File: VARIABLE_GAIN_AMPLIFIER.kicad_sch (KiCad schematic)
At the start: 33 parts, among them IC35 ${DEVICE}

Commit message: Rerouted PCB Logic part
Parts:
- renumbered C94 to C601, C95 to C602, C96 to C603, C97 to C604, C98 to C605, C99 to C606, C100 to C607, C101 to C608, C102 to C609, C103 to C610, C104 to C611, C105 to C612, C106 to C613, C107 to C614, C108 to C615, C109 to C616, C110 to C617, C621 to C619, C619 to C620, C620 to C621, FL3 to FL601, FL4 to FL602, IC35 to IC601, R73 to R601, R74 to R602, R75 to R603, R76 to R604, R77 to R605, R78 to R606, TR5 to TR601, TR6 to TR602

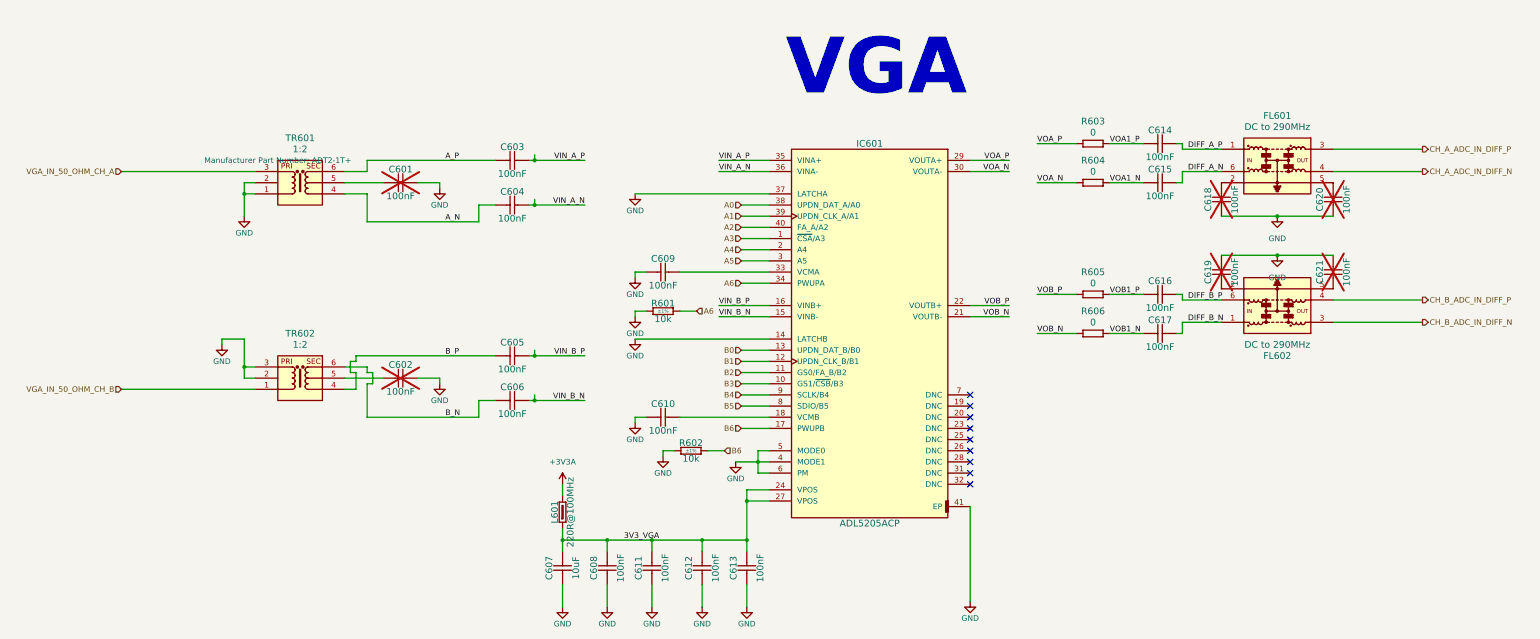
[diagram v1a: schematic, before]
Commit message: Inverted the VGA output
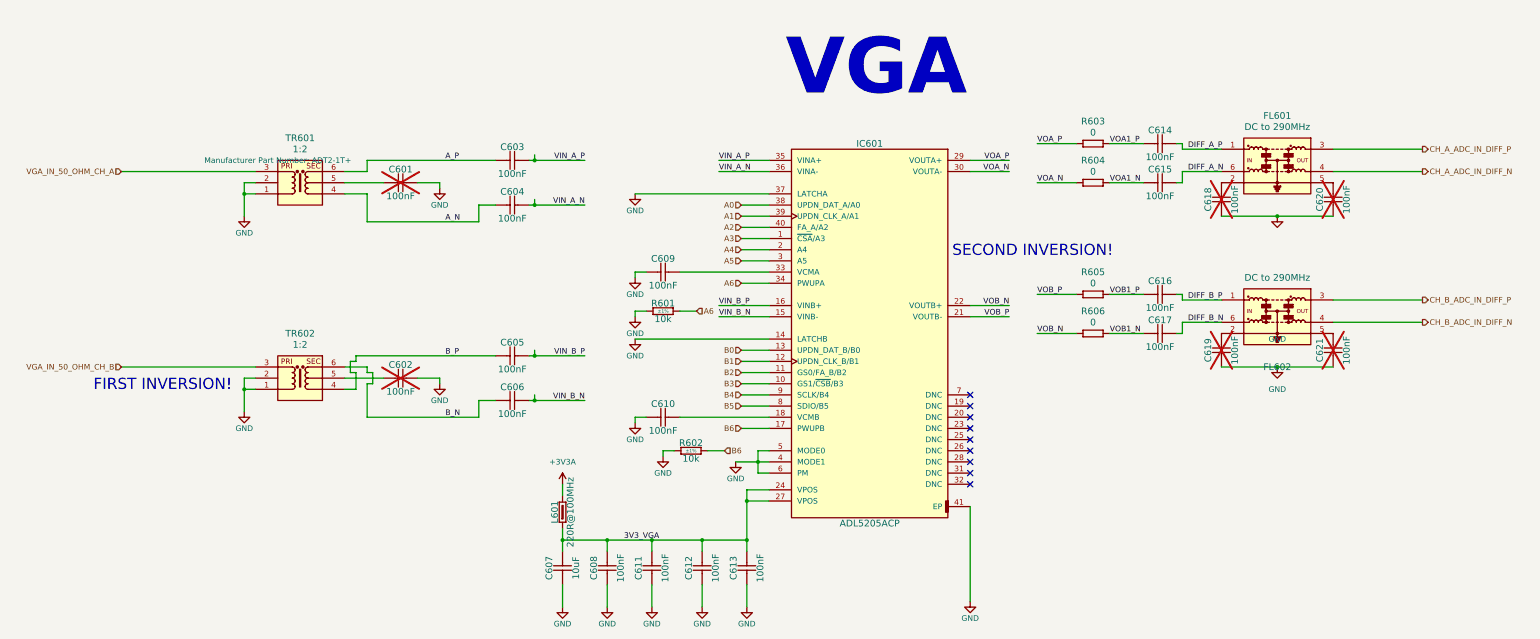
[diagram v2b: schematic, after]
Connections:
- net CH_B_ADC_IN_DIFF_N: now also FL602.4 (GND); no longer FL602.3 (RFOUT)
- net CH_B_ADC_IN_DIFF_P: now also FL602.3 (RFOUT); no longer FL602.4 (GND)
- net DIFF_B_N: now also FL602.6 (RFIN); no longer FL602.1 (RFIN)
- net DIFF_B_P: now also FL602.1 (RFIN); no longer FL602.6 (RFIN)
- net GND: now also TR602.1 (P); no longer TR602.3 (PDOT)
- net VGA_IN_50_OHM_CH_B: now also TR602.3 (PDOT); no longer TR602.1 (P)
- net VOB_N: now also IC601.22 (VOUTB+); no longer IC601.21 (VOUTB-)
- net VOB_P: now also IC601.21 (VOUTB-); no longer IC601.22 (VOUTB+)
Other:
- note added: "FIRST INVERSION!"
- note added: "SECOND INVERSION!"
- moved on the sheet: C619, C621, FL602
